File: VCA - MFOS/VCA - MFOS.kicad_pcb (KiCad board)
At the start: 2 copper layers, 101.6 x 76.2 mm, 81 parts, among them J1 CVA1, J10 LINA, J11 OUTA, J12 CVB1, J13 CVB2, J14 Sig_In_B, J15 ADJB, J16 LOGB, J17 CMNB, J18 LINB, J19 OUTB, J2 CVA2, J3 Sig_In_A, J4 ADJA, J5 +12V_Conn, J6 -12V_Conn, J7 GND_Conn, J8 LOGA, J9 CMNA, Q1 2N3904, Q2 2N3906, Q3 2N3904, Q4 2N3906, U1 TL084, U2 LM13700

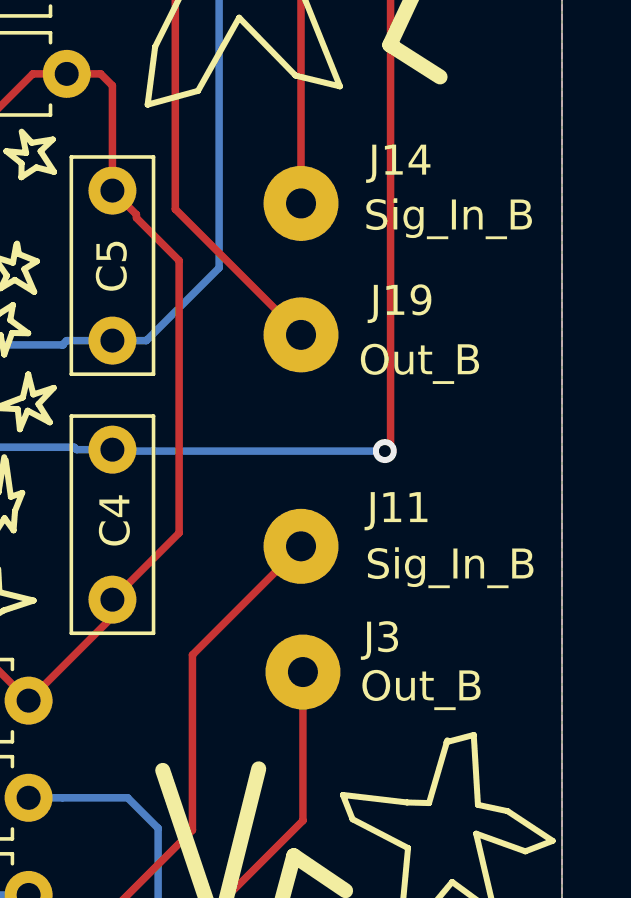
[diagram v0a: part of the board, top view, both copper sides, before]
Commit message: fixed error on silkscreen (input/output labels)
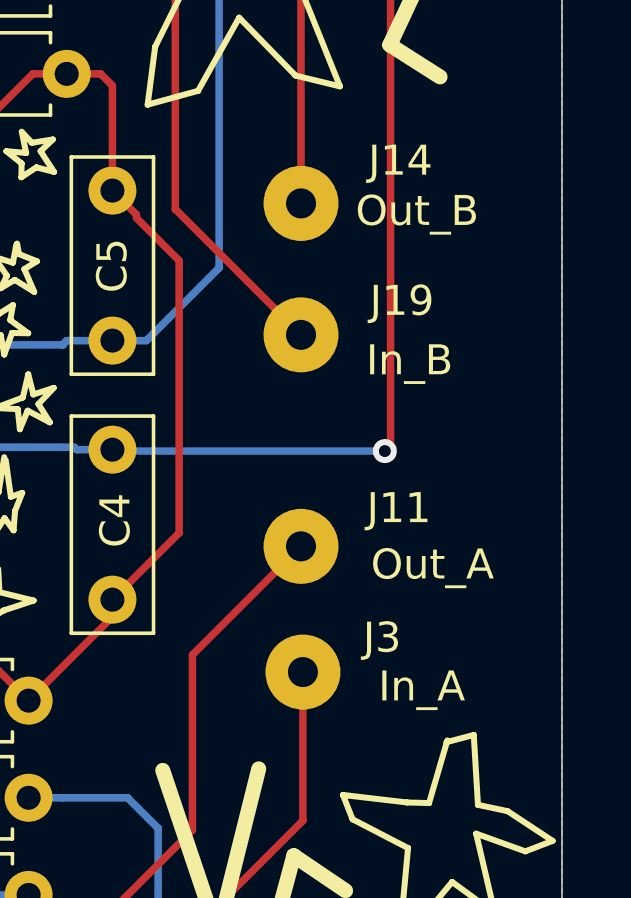
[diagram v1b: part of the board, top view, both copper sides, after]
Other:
- board text added: "In_A"
- board text added: "In_B"
- board text added: "Out_A"
- board text removed: "Sig_In_B"
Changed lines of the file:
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@@
     (effects (font (size 1 1) (thickness 0.15)))
   )
-  (gr_text Out_B (at 109.1184 60.0456) (layer F.SilkS)
-    (effects (font (size 1 1) (thickness 0.15)))
-  )
-  (gr_text Sig_In_B (at 110.0836 55.9816) (layer F.SilkS)
-    (effects (font (size 1 1) (thickness 0.15)))
-  )
-  (gr_text Out_B (at 109.0676 49.1744) (layer F.SilkS)
-    (effects (font (size 1 1) (thickness 0.15)))
-  )
-  (gr_text Sig_In_B (at 110.0328 44.3484) (layer F.SilkS)
+  (gr_text In_A (at 109.1184 60.0456) (layer F.SilkS)
+    (effects (font (size 1 1) (thickness 0.15)))
+  )
+  (gr_text Out_A (at 109.474 55.9816) (layer F.SilkS)
+    (effects (font (size 1 1) (thickness 0.15)))
+  )
+  (gr_text In_B (at 108.712 49.1744) (layer F.SilkS)
+    (effects (font (size 1 1) (thickness 0.15)))
+  )
+  (gr_text Out_B (at 108.966 44.196) (layer F.SilkS)
     (effects (font (size 1 1) (thickness 0.15)))
   )
@@
   (segment (start 53.37175 41.87825) (end 53.514 41.736) (width 0.25) (layer B.Cu) (net 1))
   (segment (start 51.562 43.688) (end 53.37175 41.87825) (width 0.25) (layer B.Cu) (net 1))
-  (segment (start 60.365538 22.247962) (end 60.365538 21.918639) (width 0.25) (layer F.Cu) (net 47))
   (segment (start 99.605999 44.313999) (end 99.605999 44.424499) (width 0.25) (layer F.Cu) (net 1))
   (segment (start 98.806 43.514) (end 99.605999 44.313999) (width 0.25) (layer F.Cu) (net 1))
@@
   (segment (start 38.227 61.087) (end 35.221602 64.092398) (width 0.25) (layer B.Cu) (net 18))
   (segment (start 53.616747 84.241753) (end 53.616747 80.182181) (width 0.25) (layer B.Cu) (net 18))
-  (segment (start 63.3095 75.1205) (end 63.3095 74.7395) (width 0.25) (layer B.Cu) (net 46))
   (segment (start 37.084 43.942) (end 37.084 46.736) (width 0.25) (layer F.Cu) (net 19))
   (segment (start 31.75 38.608) (end 37.084 43.942) (width 0.25) (layer F.Cu) (net 19))
@@
   (segment (start 100.9015 44.1325) (end 100.9015 33.3375) (width 0.25) (layer F.Cu) (net 44))
   (segment (start 105.0925 48.3235) (end 100.9015 44.1325) (width 0.25) (layer F.Cu) (net 44))
+  (segment (start 63.3095 75.1205) (end 63.3095 74.7395) (width 0.25) (layer B.Cu) (net 46))
   (segment (start 63.3095 74.7395) (end 61.5315 74.7395) (width 0.25) (layer F.Cu) (net 46))
   (segment (start 60.687994 73.895994) (end 57.377139 73.895994) (width 0.25) (layer F.Cu) (net 46))
   (segment (start 61.5315 74.7395) (end 60.687994 73.895994) (width 0.25) (layer F.Cu) (net 46))
+  (segment (start 60.365538 22.247962) (end 60.365538 21.918639) (width 0.25) (layer F.Cu) (net 47))
   (segment (start 62.304639 21.918639) (end 64.77 24.384) (width 0.25) (layer B.Cu) (net 47))
   (segment (start 60.365538 21.918639) (end 62.304639 21.918639) (width 0.25) (layer B.Cu) (net 47))
